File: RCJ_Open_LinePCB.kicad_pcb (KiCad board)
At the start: 4 copper layers, 180 x 171.9 mm, 205 parts, among them J1 Conn_01x12, U1 MCP3008, U2 MCP3008, U3 MCP3008, U4 MCP3008, U5 MCP3008, U6 MCP3008

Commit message: Finished Rerouting
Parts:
- U4, U5: moved to B.Cu
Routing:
- net GND: track 1007.6 -> 988.3 mm
- net MISO: track 324.4 -> 308.4 mm, vias 6 -> 7
- net Ch40: track 50.0 -> 64.4 mm, vias 1 -> 2
- net Ch26: track 87.1 -> 97.1 mm
- net Ch25: track 96.8 -> 106.7 mm
- net Ch33: track 23.4 -> 33.0 mm, vias 1 -> 2
- net Ch38: track 39.1 -> 47.1 mm
- net Ch39: track 39.8 -> 46.7 mm, vias 1 -> 2
- net Ch27: track 74.9 -> 81.5 mm
- net Ch34: track 12.6 -> 19.0 mm, vias 1 -> 2
- net MOSI: track 342.9 -> 348.9 mm
- net Ch31: track 52.4 -> 46.5 mm, vias 1 -> 2
- net CS4: track 137.7 -> 143.5 mm
- net Ch30: track 51.9 -> 47.3 mm
- net SCK1: track 338.8 -> 343.4 mm
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
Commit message: Finished line
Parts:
- R100, R101, R102, R97, R98, R99: moved to B.Cu

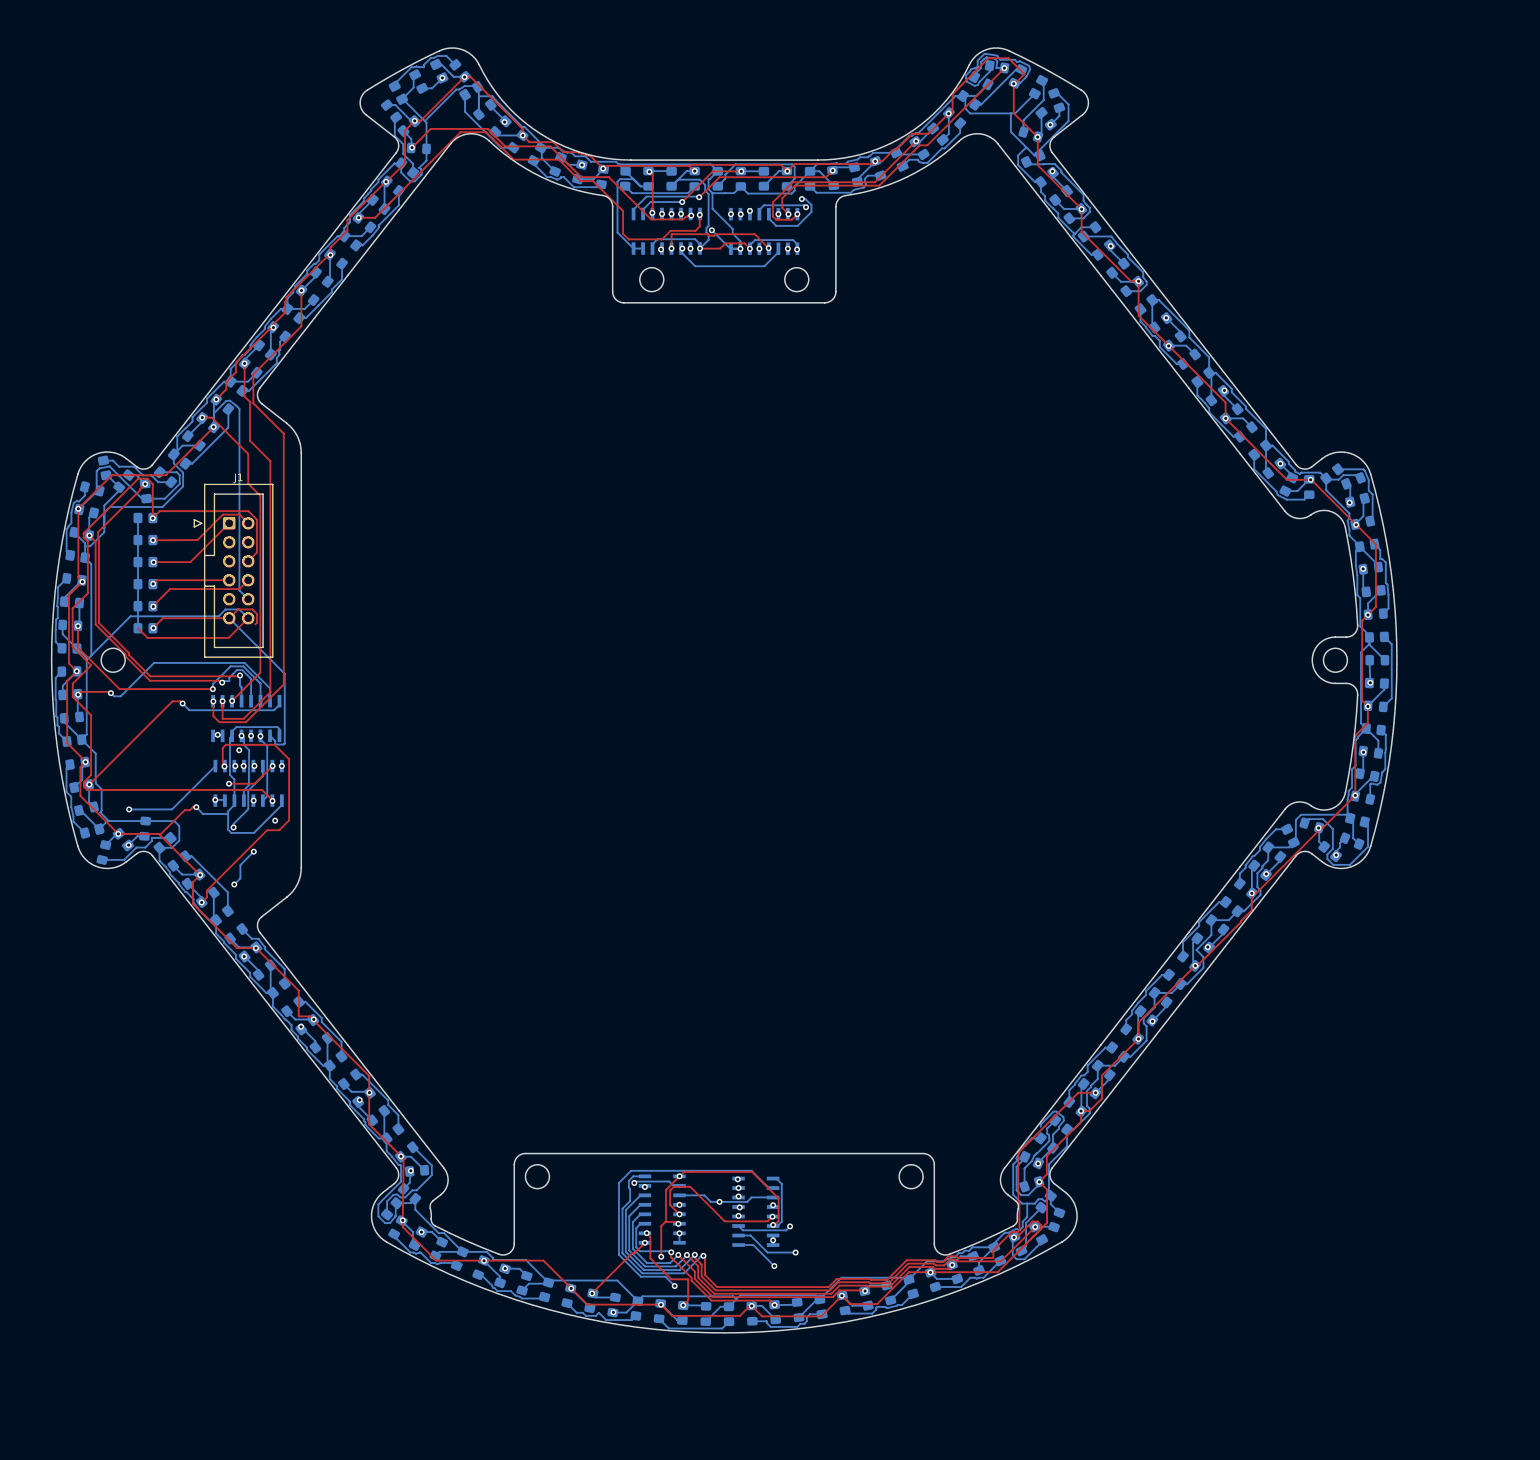
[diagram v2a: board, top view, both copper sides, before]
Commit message: Added Ground Plane
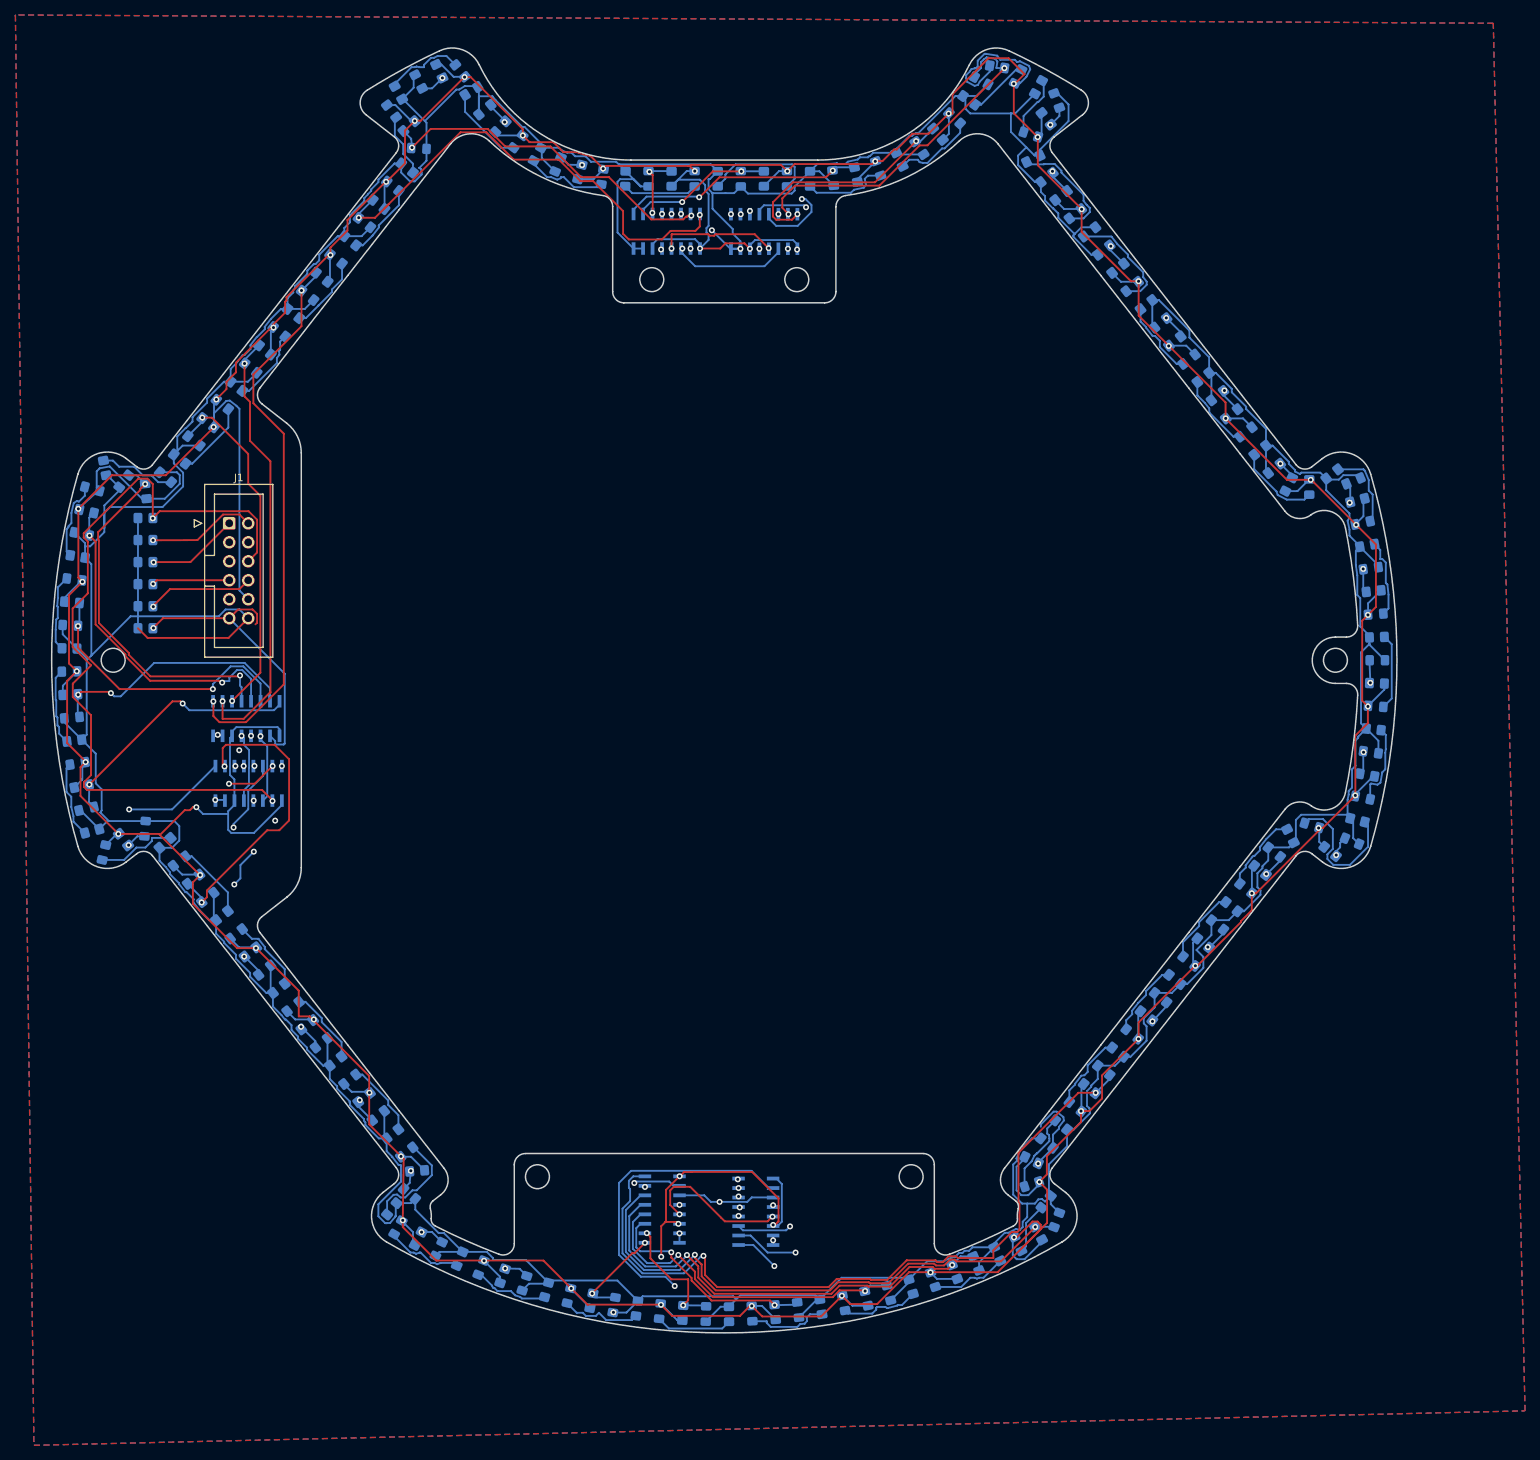
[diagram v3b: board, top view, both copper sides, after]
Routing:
- added copper zone on B.Cu, net GND
- added copper zone on F.Cu, net GND
- added copper zone on In1.Cu, net GND
- added copper zone on In2.Cu, net GND
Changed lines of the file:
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@@
 		(attr smd)
 		(fp_line
-			(start 0.999999 0.96)
+			(start 0.999998 0.96)
 			(end -1.86 0.96)
 			(stroke
@@
 		(tags "resistor handsolder")
 		(property "Reference" "R97"
-			(at 0 1.65 360)
+			(at 0 1.65 0)
 			(layer "B.SilkS")
 			(effects
@@
 		)
 		(property "Value" "10K"
-			(at 0 -1.65 360)
+			(at 0 -1.65 0)
 			(layer "B.Fab")
 			(effects
@@
 		)
 		(fp_text user "${REFERENCE}"
-			(at 0 0 360)
+			(at 0 0 0)
 			(layer "B.Fab")
 			(effects
@@
 		(tags "resistor handsolder")
 		(property "Reference" "R98"
-			(at 0 1.65 360)
+			(at 0 1.65 0)
 			(layer "B.SilkS")
 			(effects
@@
 		)
 		(property "Value" "10K"
-			(at 0 -1.65 360)
+			(at 0 -1.65 0)
 			(layer "B.Fab")
 			(effects
@@
 		)
 		(fp_text user "${REFERENCE}"
-			(at 0 0 360)
+			(at 0 0 0)
 			(layer "B.Fab")
 			(effects
@@
 		(fp_line
 			(start 1 0.96)
-			(end -1.859999 0.96)
+			(end -1.859998 0.96)
 			(stroke
 				(width 0.12)
@@
 		)
 		(fp_line
-			(start -1.859999 0.96)
+			(start -1.859998 0.96)
 			(end -1.86 -0.96)
 			(stroke
@@
 		(tags "resistor handsolder")
 		(property "Reference" "R8"
-			(at 0 1.649999 7.054126318)
+			(at 0 1.649998 7.054126318)
 			(layer "B.SilkS")
 			(effects
@@
 		)
 		(property "Value" "750"
-			(at 0 -1.649999 7.054126318)
+			(at 0 -1.649998 7.054126318)
 			(layer "B.Fab")
 			(effects
@@
 		)
 		(fp_line
-			(start -1.860001 0.96)
+			(start -1.860002 0.96)
 			(end -1.86 -0.96)
 			(stroke
@@
 		(fp_line
 			(start 1 0.96)
-			(end -1.860001 0.96)
+			(end -1.860002 0.96)
 			(stroke
 				(width 0.12)
@@
 		)
 		(fp_line
-			(start -1.849999 0.95)
+			(start -1.849998 0.95)
 			(end 1.85 0.95)
 			(stroke
@@
 		(fp_line
 			(start 1.85 0.95)
-			(end 1.849999 -0.95)
+			(end 1.849998 -0.95)
 			(stroke
 				(width 0.05)
@@
 		(fp_line
 			(start -1.85 -0.95)
-			(end -1.849999 0.95)
+			(end -1.849998 0.95)
 			(stroke
 				(width 0.05)
@@
 		)
 		(fp_line
-			(start 1.849999 -0.95)
+			(start 1.849998 -0.95)
 			(end -1.85 -0.95)
 			(stroke
@@
 		(attr smd)
 		(fp_line
-			(start -0.227064 0.734999)
+			(start -0.227064 0.734998)
 			(end 0.227064 0.735)
 			(stroke
@@
 		(fp_line
 			(start -0.227064 -0.735)
-			(end 0.227064 -0.734999)
+			(end 0.227064 -0.734998)
 			(stroke
 				(width 0.12)
@@
 		(fp_line
 			(start -1 -0.6)
-			(end 0.999999 -0.6)
+			(end 0.999998 -0.6)
 			(stroke
 				(width 0.1)
@@
 		)
 		(fp_line
-			(start 0.999999 -0.6)
+			(start 0.999998 -0.6)
 			(end 1 0.6)
 			(stroke
@@
 		(tags "resistor handsolder")
 		(property "Reference" "R99"
-			(at 0 1.65 360)
+			(at 0 1.65 0)
 			(layer "B.SilkS")
 			(effects
@@
 		)
 		(property "Value" "10K"
-			(at 0 -1.65 360)
+			(at 0 -1.65 0)
 			(layer "B.Fab")
 			(effects
@@
 		)
 		(fp_text user "${REFERENCE}"
-			(at 0 0 360)
+			(at 0 0 0)
 			(layer "B.Fab")
 			(effects
@@
 		(tags "resistor handsolder")
 		(property "Reference" "R101"
-			(at 0 1.65 360)
+			(at 0 1.65 0)
 			(layer "B.SilkS")
 			(effects
@@
 		)
 		(property "Value" "10K"
-			(at 0 -1.65 360)
+			(at 0 -1.65 0)
 			(layer "B.Fab")
 			(effects
@@
 		)
 		(fp_text user "${REFERENCE}"
-			(at 0 0 360)
+			(at 0 0 0)
 			(layer "B.Fab")
 			(effects
@@
 		)
 		(fp_line
-			(start 1 0.599999)
+			(start 1 0.599998)
 			(end -0.7 0.6)
 			(stroke
@@
 		(fp_line
 			(start 1 -0.6)
-			(end 1 0.599999)
+			(end 1 0.599998)
 			(stroke
 				(width 0.1)
@@
 		(fp_line
 			(start -1 0.3)
-			(end -1 -0.599999)
+			(end -1 -0.599998)
 			(stroke
 				(width 0.1)
@@
 		)
 		(fp_line
-			(start -1 -0.599999)
+			(start -1 -0.599998)
 			(end 1 -0.6)
 			(stroke
@@
 		)
 		(fp_line
-			(start 1.849999 0.95)
+			(start 1.849998 0.95)
 			(end 1.85 -0.95)
 			(stroke
@@
 		(fp_line
 			(start -1.85 0.95)
-			(end 1.849999 0.95)
+			(end 1.849998 0.95)
 			(stroke
 				(width 0.05)
@@
 		(fp_line
 			(start 1.85 -0.95)
-			(end -1.849999 -0.95)
+			(end -1.849998 -0.95)
 			(stroke
 				(width 0.05)
@@
 		)
 		(fp_line
-			(start -1.849999 -0.95)
+			(start -1.849998 -0.95)
 			(end -1.85 0.95)
 			(stroke
@@
 		)
 		(fp_text user "*"
-			(at -2.5654 6.096 360)
+			(at -2.5654 6.096 0)
 			(layer "B.SilkS")
 			(effects
@@
 		)
 		(fp_text user "*"
-			(at -1.5748 4.8768 360)
+			(at -1.5748 4.8768 0)
 			(layer "B.Fab")
 			(effects
@@
 		(tags "resistor handsolder")
 		(property "Reference" "R100"
-			(at 0 1.65 360)
+			(at 0 1.65 0)
 			(layer "B.SilkS")
 			(effects
@@
 		)
 		(property "Value" "10K"
-			(at 0 -1.65 360)
+			(at 0 -1.65 0)
 			(layer "B.Fab")
 			(effects
@@
 		)
 		(fp_text user "${REFERENCE}"
-			(at 0 0 360)
+			(at 0 0 0)
 			(layer "B.Fab")
 			(effects
@@
 		)
 		(fp_line
-			(start -1.850001 -0.95)
+			(start -1.850002 -0.95)
 			(end -1.85 0.95)
 			(stroke
@@
 		(fp_line
 			(start -1.85 0.95)
-			(end 1.850001 0.95)
+			(end 1.850002 0.95)
 			(stroke
 				(width 0.05)
@@
 		(fp_line
 			(start 1.85 -0.95)
-			(end -1.850001 -0.95)
+			(end -1.850002 -0.95)
 			(stroke
 				(width 0.05)
@@
 		)
 		(fp_line
-			(start 1.850001 0.95)
+			(start 1.850002 0.95)
 			(end 1.85 -0.95)
 			(stroke
@@
 		(tags "resistor handsolder")
 		(property "Reference" "R102"
-			(at 0 1.65 360)
+			(at 0 1.65 0)
 			(layer "B.SilkS")
 			(effects
@@
 		)
 		(property "Value" "10K"
-			(at 0 -1.65 360)
+			(at 0 -1.65 0)
 			(layer "B.Fab")
 			(effects
@@
 		)
 		(fp_text user "${REFERENCE}"
-			(at 0 0 360)
+			(at 0 0 0)
 			(layer "B.Fab")
 			(effects
@@
 		)
 		(fp_line
-			(start -1.850001 0.95)
+			(start -1.850002 0.95)
 			(end 1.85 0.95)
 			(stroke
@@
 		(fp_line
 			(start -1.85 -0.95)
-			(end -1.850001 0.95)
+			(end -1.850002 0.95)
 			(stroke
 				(width 0.05)
@@
 		(fp_line
 			(start 1.85 0.95)
-			(end 1.850001 -0.95)
+			(end 1.850002 -0.95)
 			(stroke
 				(width 0.05)
@@
 		)
 		(fp_line
-			(start 1.850001 -0.95)
+			(start 1.850002 -0.95)
 			(end -1.85 -0.95)
 			(stroke
@@
 		(fp_line
 			(start -0.227064 -0.735)
-			(end 0.227063 -0.735)
+			(end 0.227062 -0.735)
 			(stroke
 				(width 0.12)
@@
 		)
 		(fp_line
-			(start -0.227063 0.735)
+			(start -0.227062 0.735)
 			(end 0.227064 0.735)
 			(stroke
@@
 	)
 	(segment
-		(start 145.535986 19.73992)
-		(end 142.837424 22.438482)
+		(start 144.819653 19.985337)
+		(end 144.714663 19.985337)
 		(width 0.25)
 		(layer "B.Cu")
@@
 	)
 	(segment
-		(start 142.837424 22.438482)
-		(end 142.837424 24.016394)
+		(start 145.318091 17.130941)
+		(end 145.535986 17.348836)
 		(width 0.25)
 		(layer "B.Cu")
@@
 	)
 	(segment
-		(start 145.318091 17.130941)
-		(end 145.535986 17.348836)
+		(start 144.714663 19.985337)
+		(end 142.837424 21.862576)
 		(width 0.25)
 		(layer "B.Cu")
@@
 	(segment
 		(start 145.535986 17.348836)
-		(end 145.535986 19.73992)
+		(end 145.535986 19.269004)
+		(width 0.25)
+		(layer "B.Cu")
+		(net 73)
+	)
+	(segment
+		(start 145.535986 19.269004)
+		(end 144.819653 19.985337)
+		(width 0.25)
+		(layer "B.Cu")
+		(net 73)
+	)
+	(segment
+		(start 142.837424 21.862576)
+		(end 142.837424 24.016394)
 		(width 0.25)
 		(layer "B.Cu")
@@
 		(net 108)
 	)
+	(zone
+		(net 1)
+		(net_name "GND")
+		(layers "F.Cu" "In1.Cu" "In2.Cu" "B.Cu")
+		(hatch edge 0.5)
+		(connect_pads
+			(clearance 0.508)
+		)
+		(min_thickness 0.25)
+		(filled_areas_thickness no)
+		(fill yes
+			(thermal_gap 0.5)
+			(thermal_bridge_width 0.5)
+		)
+		(polygon
+			(pts
+				(xy 7.95 8.39) (xy 10.43 199.72) (xy 209.94 195.11) (xy 205.69 9.45) (xy 7.89 8.34)
+			)
+		)
+	)
 	(group ""

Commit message: Added GND plane
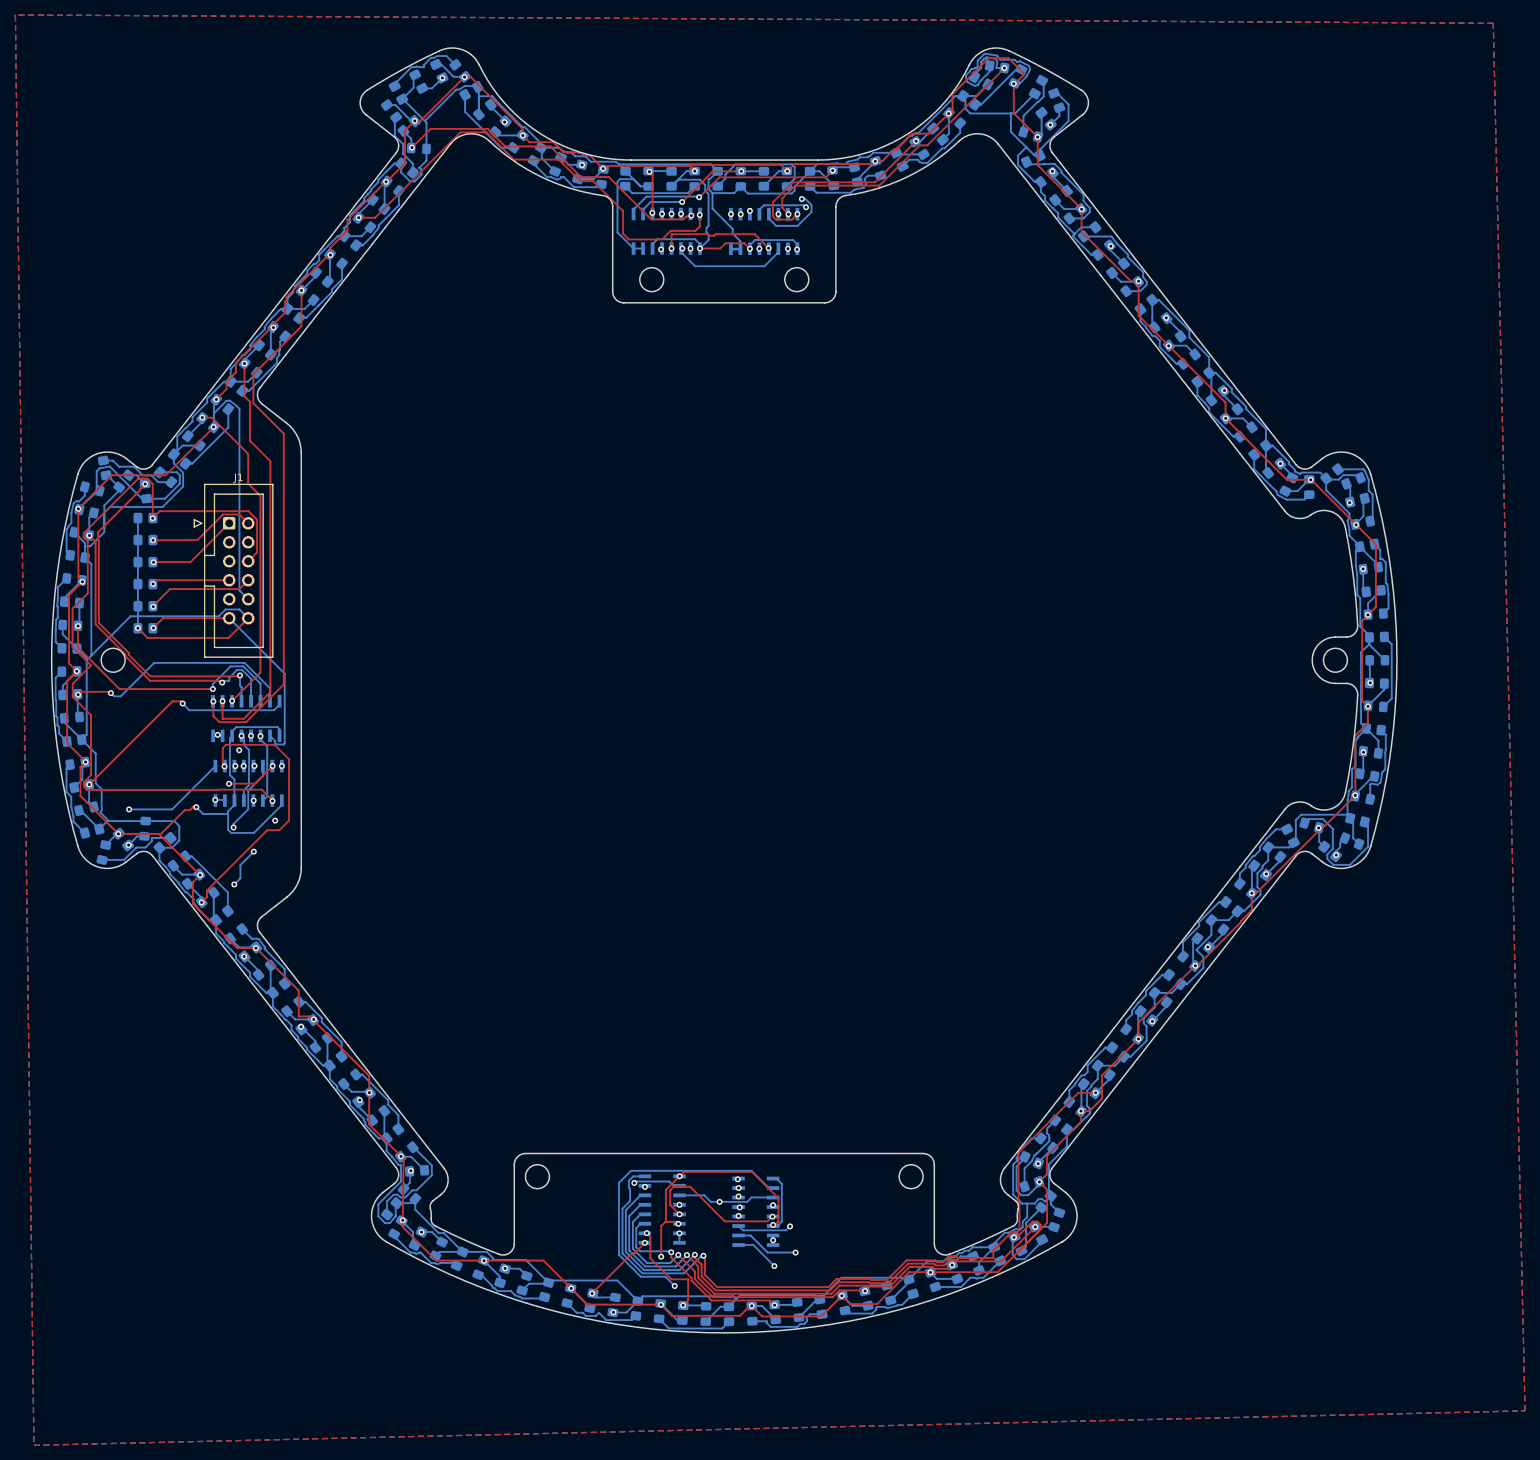
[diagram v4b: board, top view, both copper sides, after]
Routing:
- net Ch15: track 85.2 -> 76.2 mm
- net CS6: track 39.4 -> 33.4 mm
- net 3.3V: track 945.9 -> 942.4 mm, vias 7 -> 6
- net MOSI: track 348.9 -> 345.5 mm
- net Ch40: track 64.4 -> 63.7 mm
